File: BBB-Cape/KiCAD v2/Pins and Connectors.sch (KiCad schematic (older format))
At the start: 8 parts, among them J9 01x06_Stackable Header, P1 02x23_Stackable Header, P2 02x23_Stackable Header, SW1 W5500_RST, SW2 SYS_RST, SW3 Power

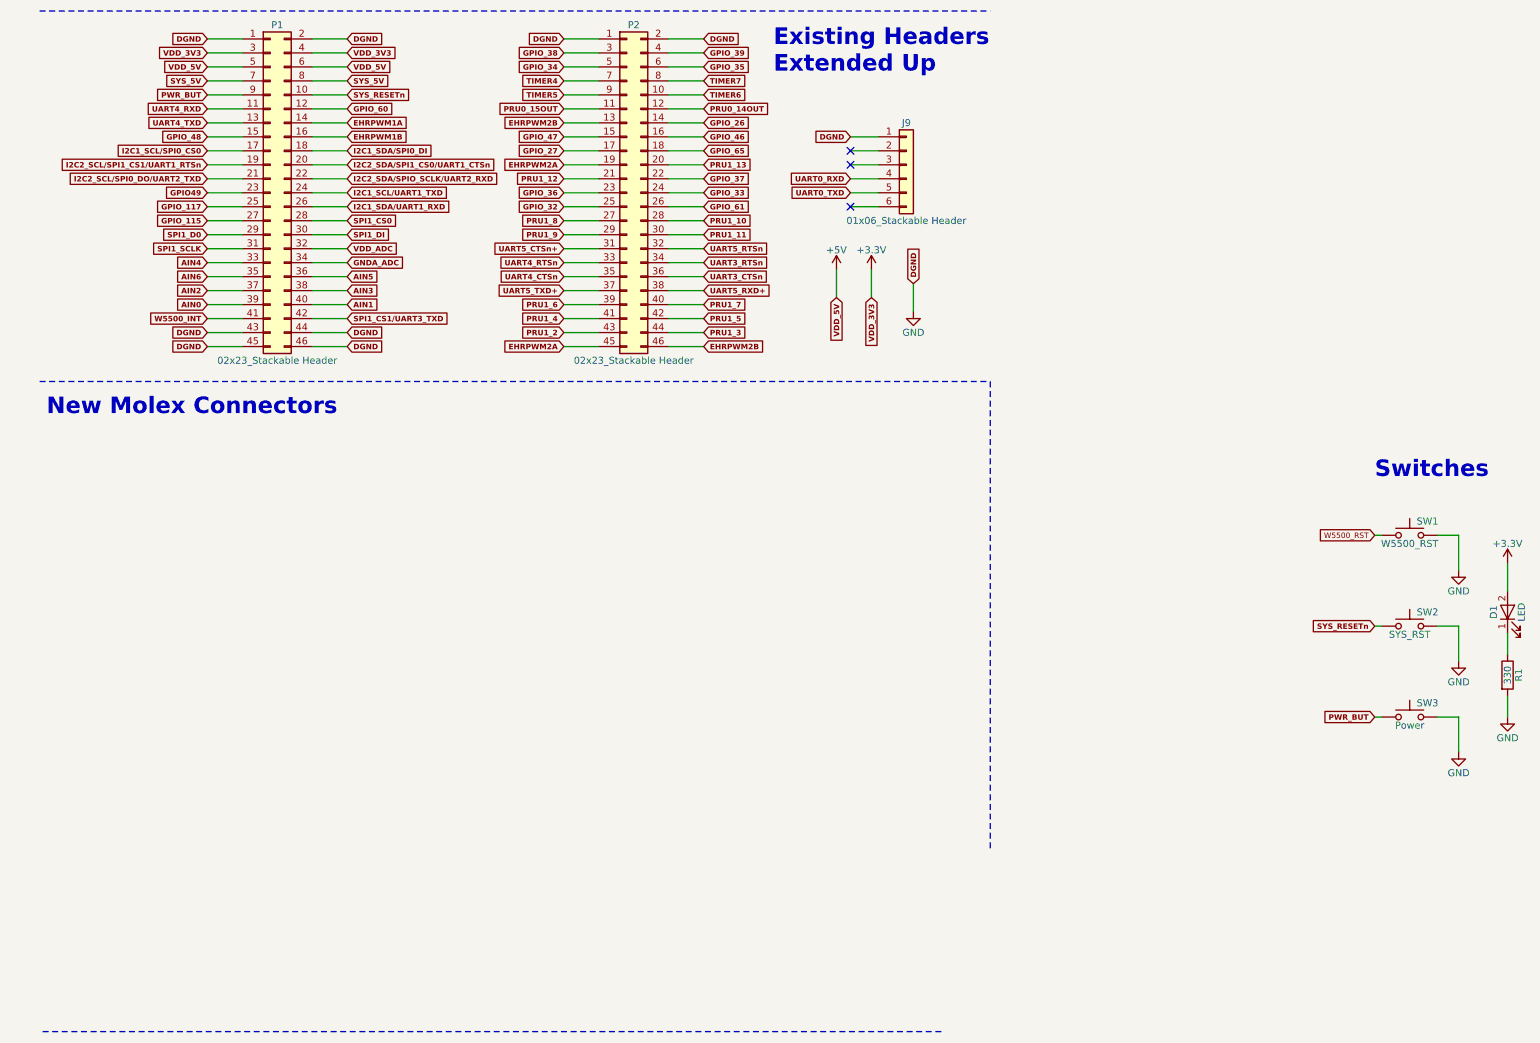
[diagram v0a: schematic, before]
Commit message: Schematic Rework for Rev3
Updated schematic based on Ed changes / review.
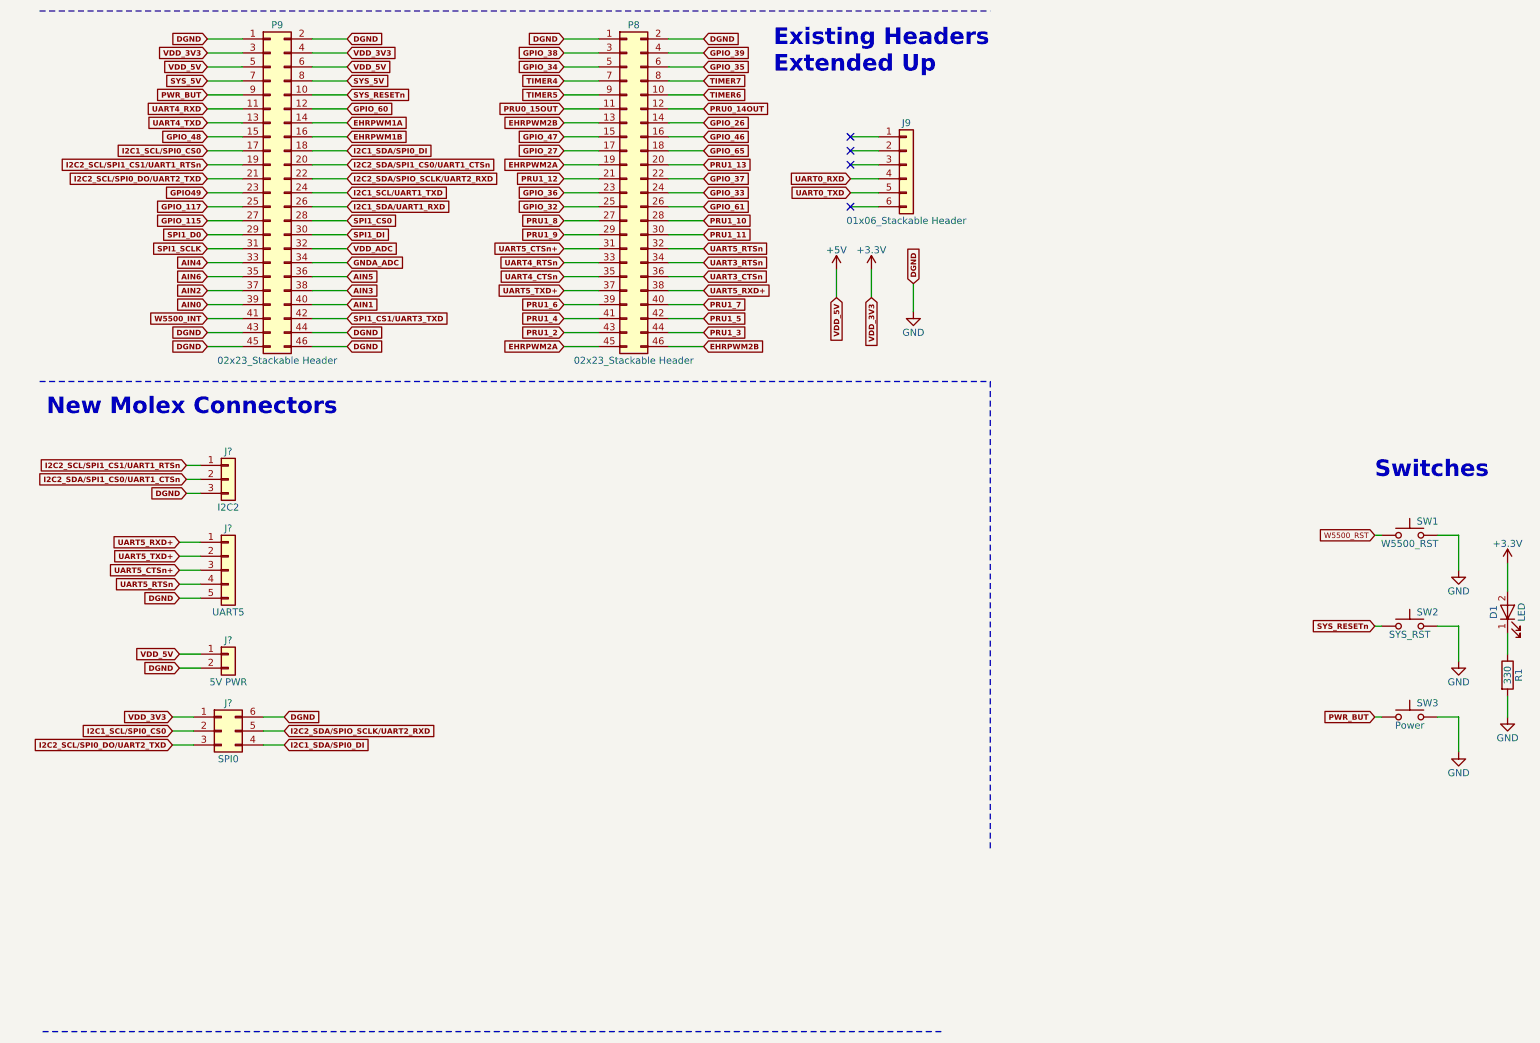
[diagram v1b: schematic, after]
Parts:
- added J?: I2C2, symbol Conn_01x03
- added J?: 5V PWR, symbol Conn_01x02
- added J?: SPI0, symbol Conn_02x03_Counter_Clockwise
- added J?: UART5, symbol Conn_01x05
- renumbered P2 to P8, P1 to P9
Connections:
- net +3V3: now also J?.1 (Pin_1)
- net +5V: now also J?.1 (Pin_1)
- net GND: now also J?.2 (Pin_2), J?.3 (Pin_3), J?.5 (Pin_5), J?.6 (Pin_6); no longer J9.1 (Pin_1)
- net I2C1_SCL/SPI0_CS0: now also J?.2 (Pin_2)
- net I2C1_SDA/SPI0_DI: now also J?.4 (Pin_4)
- net I2C2_SCL/SPI0_DO/UART2_TXD: now also J?.3 (Pin_3)
- net I2C2_SCL/SPI1_CS1/UART1_RTSn: now also J?.1 (Pin_1)
- net I2C2_SDA/SPI1_CS0/UART1_CTSn: now also J?.2 (Pin_2)
- net I2C2_SDA/SPIO_SCLK/UART2_RXD: now also J?.5 (Pin_5)
- net UART5_CTSn+: now also J?.3 (Pin_3)
- net UART5_RTSn: now also J?.4 (Pin_4)
- net UART5_RXD+: now also J?.1 (Pin_1)
- net UART5_TXD+: now also J?.2 (Pin_2)
- no-connect marks 3 -> 4
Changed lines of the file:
@@
 $EndDescr
 $Comp
-L Conn_02x23_Odd_Even P1
+L Conn_02x23_Odd_Even P9
 U 1 1 5A08F22D
 P 2150 1800
-F 0 "P1" H 2200 3000 50  0000 C CNN
+F 0 "P9" H 2200 3000 50  0000 C CNN
 F 1 "02x23_Stackable Header" H 2200 600 50  0000 C CNN
 F 2 "Pin_Headers:Pin_Header_Straight_2x23_Pitch2.54mm" H 2150 1800 50  0001 C CNN
@@
 $EndComp
 $Comp
-L Conn_02x23_Odd_Even P2
+L Conn_02x23_Odd_Even P8
 U 1 1 5A08F9A9
 P 4700 1800
-F 0 "P2" H 4750 3000 50  0000 C CNN
+F 0 "P8" H 4750 3000 50  0000 C CNN
 F 1 "02x23_Stackable Header" H 4750 600 50  0000 C CNN
 F 2 "Pin_Headers:Pin_Header_Straight_2x23_Pitch2.54mm" H 4700 1800 50  0001 C CNN
@@
 Text GLabel 6300 1700 0    39   Input ~ 8
 UART0_RXD
-Text GLabel 6300 1400 0    39   Input ~ 8
-DGND
 NoConn ~ 6300 1500
 NoConn ~ 6300 1600
@@
 Wire Notes Line
 	7300 3150 7300 6500
+$Comp
+L Conn_01x03 J?
+U 1 1 5A56B174
+P 1850 3850
+F 0 "J?" H 1850 4050 50  0000 C CNN
+F 1 "I2C2" H 1850 3650 50  0000 C CNN
+F 2 "" H 1850 3850 50  0001 C CNN
+F 3 "" H 1850 3850 50  0001 C CNN
+	1    1850 3850
+	1    0    0    -1
+$EndComp
+$Comp
+L Conn_01x02 J?
+U 1 1 5A56B1D7
+P 1850 5100
+F 0 "J?" H 1850 5200 50  0000 C CNN
+F 1 "5V PWR" H 1850 4900 50  0000 C CNN
+F 2 "" H 1850 5100 50  0001 C CNN
+F 3 "" H 1850 5100 50  0001 C CNN
+	1    1850 5100
+	1    0    0    -1
+$EndComp
+$Comp
+L Conn_02x03_Counter_Clockwise J?
+U 1 1 5A56B285
+P 1800 5650
+F 0 "J?" H 1850 5850 50  0000 C CNN
+F 1 "SPI0" H 1850 5450 50  0000 C CNN
+F 2 "" H 1800 5650 50  0001 C CNN
+F 3 "" H 1800 5650 50  0001 C CNN
+	1    1800 5650
+	1    0    0    -1
+$EndComp
+Text GLabel 1550 3750 0    39   Input ~ 8
+I2C2_SCL/SPI1_CS1/UART1_RTSn
+Wire Wire Line
+	1650 3750 1550 3750
+Text GLabel 1550 3850 0    39   Input ~ 8
+I2C2_SDA/SPI1_CS0/UART1_CTSn
+Wire Wire Line
+	1650 3850 1550 3850
+Text GLabel 1550 3950 0    39   Input ~ 8
+DGND
+Wire Wire Line
+	1650 3950 1550 3950
+Text GLabel 1450 5550 0    39   Input ~ 8
+VDD_3V3
+Text GLabel 2250 5550 2    39   Input ~ 8
+DGND
+Text GLabel 1450 5650 0    39   Input ~ 8
+I2C1_SCL/SPI0_CS0
+Text GLabel 1450 5750 0    39   Input ~ 8
+I2C2_SCL/SPI0_DO/UART2_TXD
+Text GLabel 2250 5750 2    39   Input ~ 8
+I2C1_SDA/SPI0_DI
+Text GLabel 2250 5650 2    39   Input ~ 8
+I2C2_SDA/SPIO_SCLK/UART2_RXD
+Wire Wire Line
+	1450 5550 1600 5550
+Wire Wire Line
+	1600 5650 1450 5650
+Wire Wire Line
+	1450 5750 1600 5750
+Wire Wire Line
+	2250 5550 2100 5550
+Wire Wire Line
+	2100 5650 2250 5650
+Wire Wire Line
+	2250 5750 2100 5750
+$Comp
+L Conn_01x05 J?
+U 1 1 5A5706AE
+P 1850 4500
+F 0 "J?" H 1850 4800 50  0000 C CNN
+F 1 "UART5" H 1850 4200 50  0000 C CNN
+F 2 "" H 1850 4500 50  0001 C CNN
+F 3 "" H 1850 4500 50  0001 C CNN
+	1    1850 4500
+	1    0    0    -1
+$EndComp
+Text GLabel 1500 4700 0    39   Input ~ 8
+DGND
+Text GLabel 1500 4300 0    39   Input ~ 8
+UART5_RXD+
+Text GLabel 1500 4400 0    39   Input ~ 8
+UART5_TXD+
+Text GLabel 1500 4500 0    39   Input ~ 8
+UART5_CTSn+
+Text GLabel 1500 4600 0    39   Input ~ 8
+UART5_RTSn
+Wire Wire Line
+	1650 4700 1500 4700
+Wire Wire Line
+	1500 4600 1650 4600
+Wire Wire Line
+	1650 4500 1500 4500
+Wire Wire Line
+	1500 4400 1650 4400
+Wire Wire Line
+	1650 4300 1500 4300
+Wire Wire Line
+	1650 5100 1500 5100
+Text GLabel 1500 5100 0    39   Input ~ 8
+VDD_5V
+Wire Wire Line
+	1650 5200 1500 5200
+Text GLabel 1500 5200 0    39   Input ~ 8
+DGND
+NoConn ~ 6300 1400
 $EndSCHEMATC

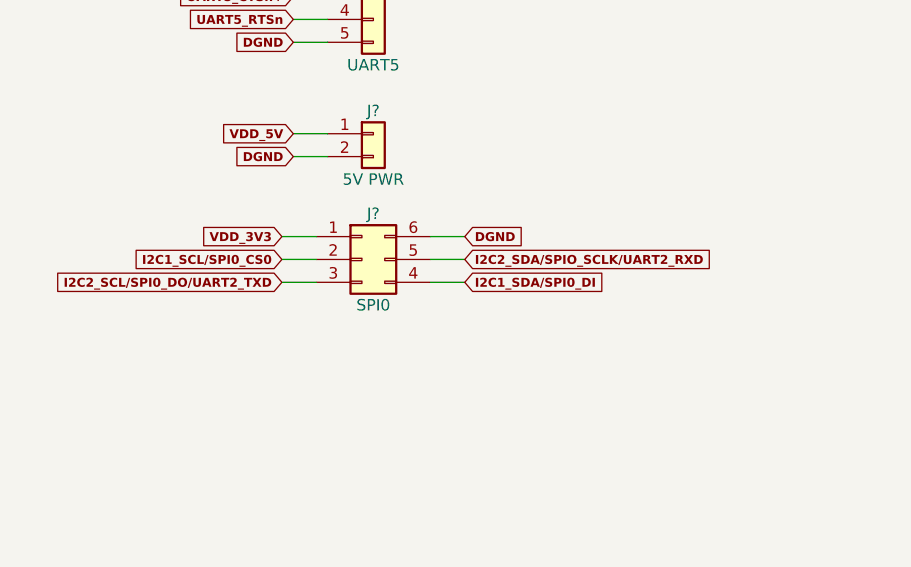
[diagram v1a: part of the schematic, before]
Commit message: Schematic Update
Updated pin mapping as described by Ed.
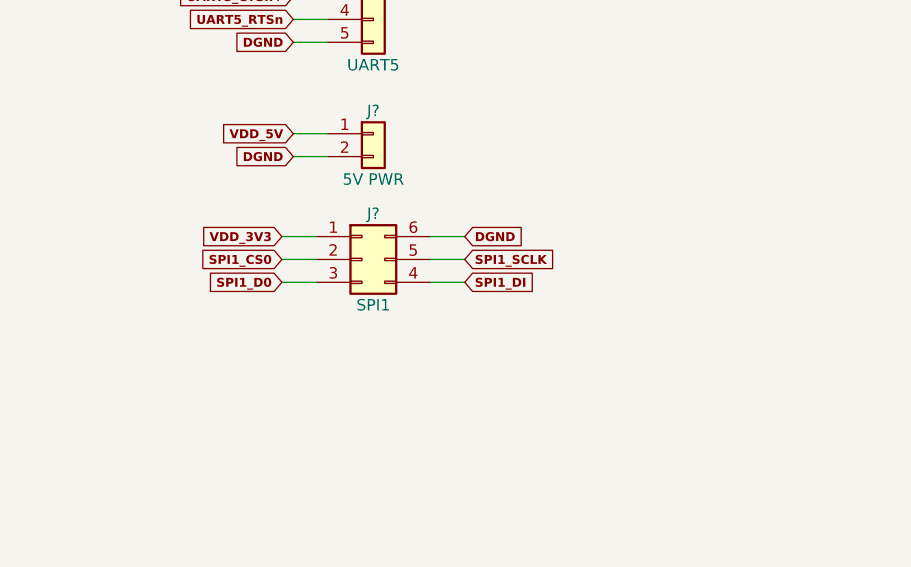
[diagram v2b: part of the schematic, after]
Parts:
- J?: value SPI0 -> SPI1
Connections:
- net I2C1_SCL/SPI0_CS0: no longer J?.2 (Pin_2)
- net I2C1_SDA/SPI0_DI: no longer J?.4 (Pin_4)
- net I2C2_SCL/SPI0_DO/UART2_TXD: no longer J?.3 (Pin_3)
- net I2C2_SDA/SPIO_SCLK/UART2_RXD: no longer J?.5 (Pin_5)
- net SPI1_CS0: now also J?.2 (Pin_2)
- net SPI1_D0: now also J?.3 (Pin_3)
- net SPI1_DI: now also J?.4 (Pin_4)
- net SPI1_SCLK: now also J?.5 (Pin_5)
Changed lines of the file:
@@
 P 1800 5650
 F 0 "J?" H 1850 5850 50  0000 C CNN
-F 1 "SPI0" H 1850 5450 50  0000 C CNN
+F 1 "SPI1" H 1850 5450 50  0000 C CNN
 F 2 "" H 1800 5650 50  0001 C CNN
 F 3 "" H 1800 5650 50  0001 C CNN
@@
 Text GLabel 2250 5550 2    39   Input ~ 8
 DGND
-Text GLabel 1450 5650 0    39   Input ~ 8
-I2C1_SCL/SPI0_CS0
-Text GLabel 1450 5750 0    39   Input ~ 8
-I2C2_SCL/SPI0_DO/UART2_TXD
-Text GLabel 2250 5750 2    39   Input ~ 8
-I2C1_SDA/SPI0_DI
-Text GLabel 2250 5650 2    39   Input ~ 8
-I2C2_SDA/SPIO_SCLK/UART2_RXD
 Wire Wire Line
 	1450 5550 1600 5550
@@
 DGND
 NoConn ~ 6300 1400
+Text GLabel 1450 5650 0    39   Input ~ 8
+SPI1_CS0
+Text GLabel 1450 5750 0    39   Input ~ 8
+SPI1_D0
+Text GLabel 2250 5750 2    39   Input ~ 8
+SPI1_DI
+Text GLabel 2250 5650 2    39   Input ~ 8
+SPI1_SCLK
 $EndSCHEMATC

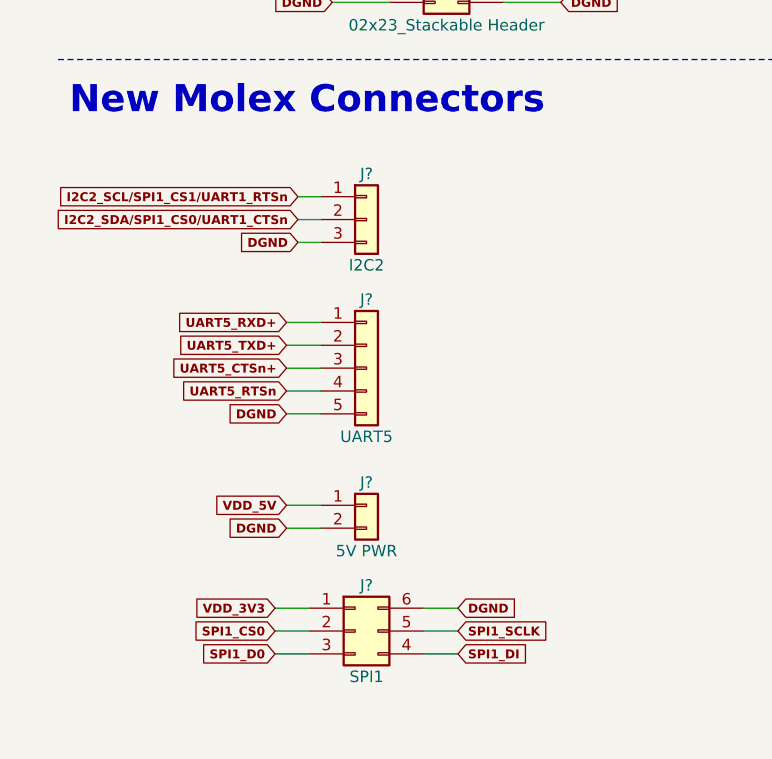
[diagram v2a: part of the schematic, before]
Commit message: Layout Update
Changed RJ45 connector to a surface mount component. Need to properly reposition P8 and P9.
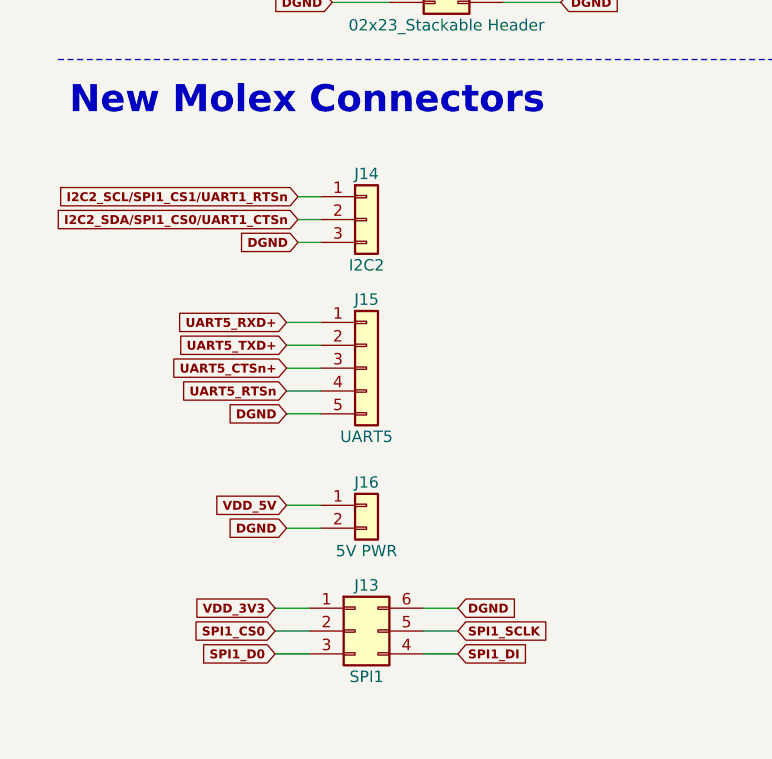
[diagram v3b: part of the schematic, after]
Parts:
- D1: footprint LEDs:LED_0805 -> LEDs:LED_0603
- J13: renamed from J?; footprint (none) -> Connectors_Molex:Molex_Microfit3_Header_02x03_Straight_43045-0628
- J14: renamed from J?; footprint (none) -> Pin_Headers:Pin_Header_Straight_1x02_Pitch2.54mm_SMD_Pin1Right
- J15: renamed from J?; footprint (none) -> Pin_Headers:Pin_Header_Straight_1x05_Pitch2.54mm_SMD_Pin1Left
- J16: renamed from J?; footprint (none) -> Connectors_Molex:Molex_KK-6410-02_02x2.54mm_Straight
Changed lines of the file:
@@
 F 0 "D1" H 11000 4900 50  0000 C CNN
 F 1 "LED" H 11000 4700 50  0000 C CNN
-F 2 "LEDs:LED_0805" H 11000 4800 50  0001 C CNN
+F 2 "LEDs:LED_0603" H 11000 4800 50  0001 C CNN
 F 3 "" H 11000 4800 50  0001 C CNN
 	1    11000 4800
@@
 	7300 3150 7300 6500
 $Comp
-L Conn_01x03 J?
+L Conn_01x03 J14
 U 1 1 5A56B174
 P 1850 3850
-F 0 "J?" H 1850 4050 50  0000 C CNN
+F 0 "J14" H 1850 4050 50  0000 C CNN
 F 1 "I2C2" H 1850 3650 50  0000 C CNN
-F 2 "" H 1850 3850 50  0001 C CNN
+F 2 "Pin_Headers:Pin_Header_Straight_1x02_Pitch2.54mm_SMD_Pin1Right" H 1850 3850 50  0001 C CNN
 F 3 "" H 1850 3850 50  0001 C CNN
 	1    1850 3850
@@
 $EndComp
 $Comp
-L Conn_01x02 J?
+L Conn_01x02 J16
 U 1 1 5A56B1D7
 P 1850 5100
-F 0 "J?" H 1850 5200 50  0000 C CNN
+F 0 "J16" H 1850 5200 50  0000 C CNN
 F 1 "5V PWR" H 1850 4900 50  0000 C CNN
-F 2 "" H 1850 5100 50  0001 C CNN
+F 2 "Connectors_Molex:Molex_KK-6410-02_02x2.54mm_Straight" H 1850 5100 50  0001 C CNN
 F 3 "" H 1850 5100 50  0001 C CNN
 	1    1850 5100
@@
 $EndComp
 $Comp
-L Conn_02x03_Counter_Clockwise J?
+L Conn_02x03_Counter_Clockwise J13
 U 1 1 5A56B285
 P 1800 5650
-F 0 "J?" H 1850 5850 50  0000 C CNN
+F 0 "J13" H 1850 5850 50  0000 C CNN
 F 1 "SPI1" H 1850 5450 50  0000 C CNN
-F 2 "" H 1800 5650 50  0001 C CNN
+F 2 "Connectors_Molex:Molex_Microfit3_Header_02x03_Straight_43045-0628" H 1800 5650 50  0001 C CNN
 F 3 "" H 1800 5650 50  0001 C CNN
 	1    1800 5650
@@
 	2250 5750 2100 5750
 $Comp
-L Conn_01x05 J?
+L Conn_01x05 J15
 U 1 1 5A5706AE
 P 1850 4500
-F 0 "J?" H 1850 4800 50  0000 C CNN
+F 0 "J15" H 1850 4800 50  0000 C CNN
 F 1 "UART5" H 1850 4200 50  0000 C CNN
-F 2 "" H 1850 4500 50  0001 C CNN
+F 2 "Pin_Headers:Pin_Header_Straight_1x05_Pitch2.54mm_SMD_Pin1Left" H 1850 4500 50  0001 C CNN
 F 3 "" H 1850 4500 50  0001 C CNN
 	1    1850 4500
